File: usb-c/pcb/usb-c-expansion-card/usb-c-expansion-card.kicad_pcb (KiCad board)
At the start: 4 copper layers, 26 x 30 mm, 15 parts, among them J1 USB_C_Receptacle, P1 USB_C_Plug, U1 USBLC6-2SC6, U2 USBLC6-2SC6, U3 USBLC6-2SC6

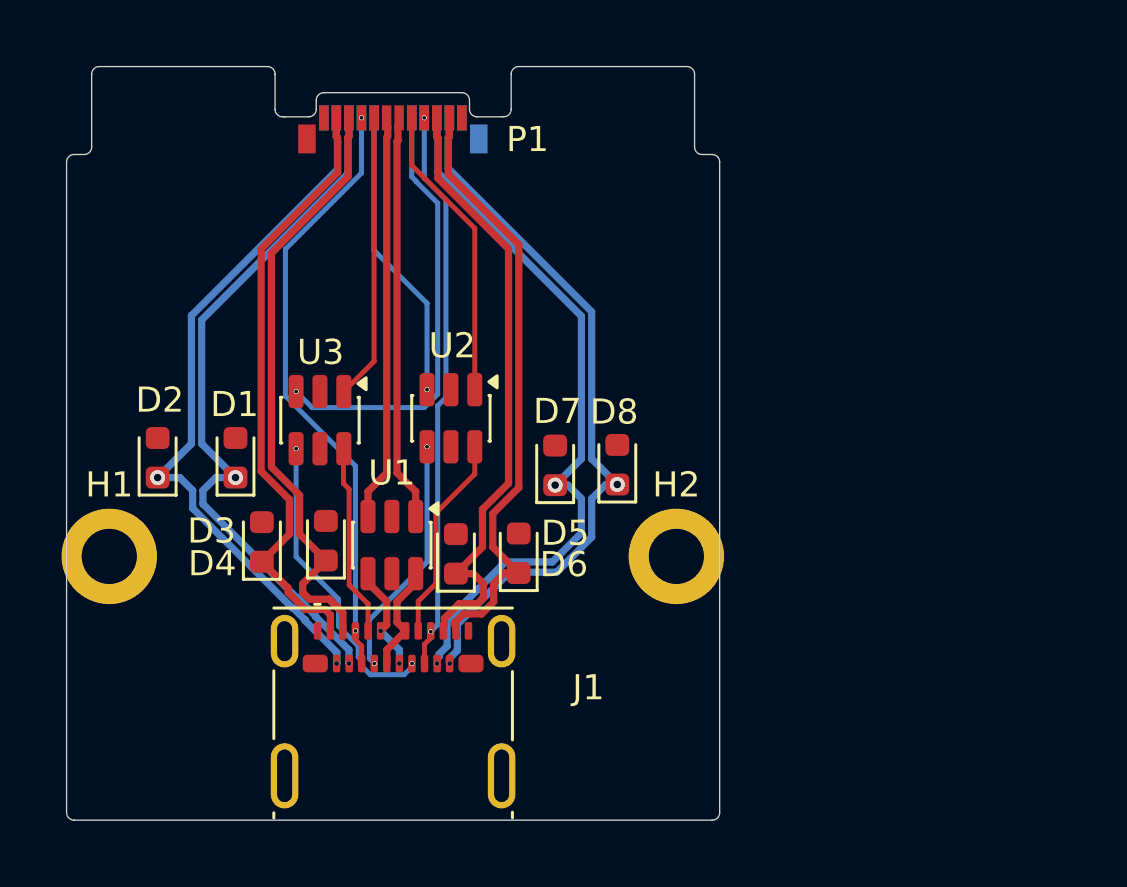
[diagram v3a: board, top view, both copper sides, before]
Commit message: routing corrected after moving footprints
Board outline was malformed, which meant moving some
stuff around and changing some traces

Signed-off-by: Lucy <user@domain.tld>
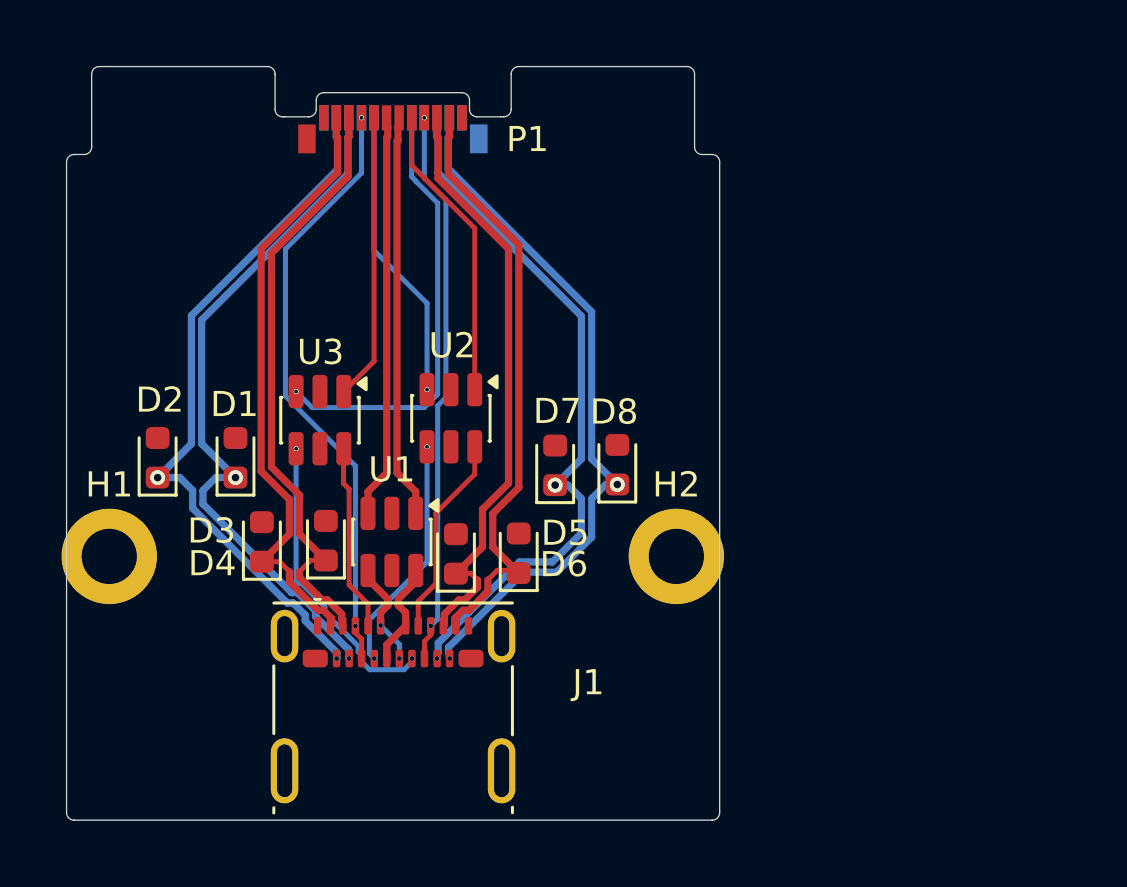
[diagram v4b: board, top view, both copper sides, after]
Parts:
- moved J1 0.20 mm to (140.0, 152.5)
- moved U1 0.12 mm to (139.9, 145.9)
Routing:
- net /ESD_RX2_N: track 24.4 -> 23.7 mm
- net /ESD_TX1_N: track 24.6 -> 24.0 mm
- net /ESD_TX2_N: track 28.8 -> 28.2 mm

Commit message: Only silkscreen graphics/text and vias missing
Signed-off-by: Lucy <user@domain.tld>
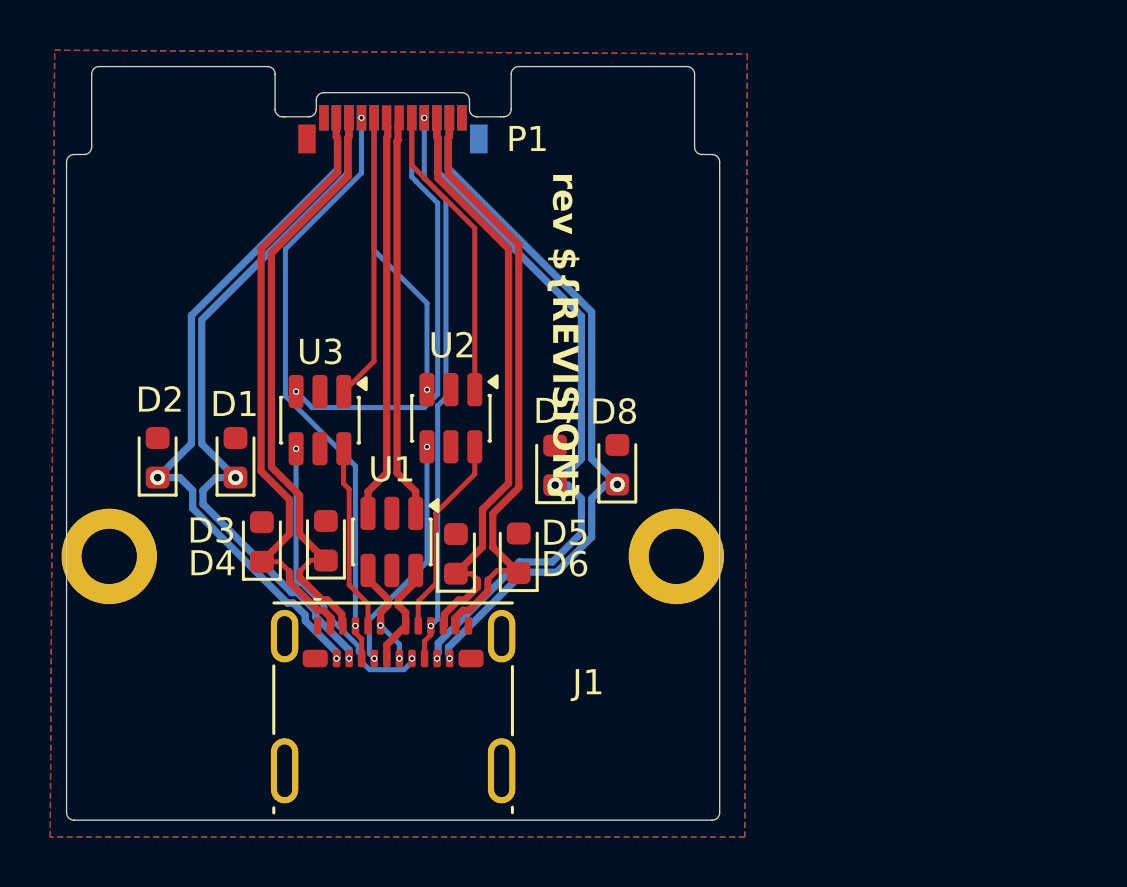
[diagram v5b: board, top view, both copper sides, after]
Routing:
- added copper zone on B.Cu, net GND
- added copper zone on F.Cu, net GND
- added copper zone on In1.Cu, net GND
- added copper zone on In2.Cu, net GND
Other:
- board text added: "rev ${REVISION}"

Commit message: Add text and graphics to silkscreen
Signed-off-by: Lucy <user@domain.tld>
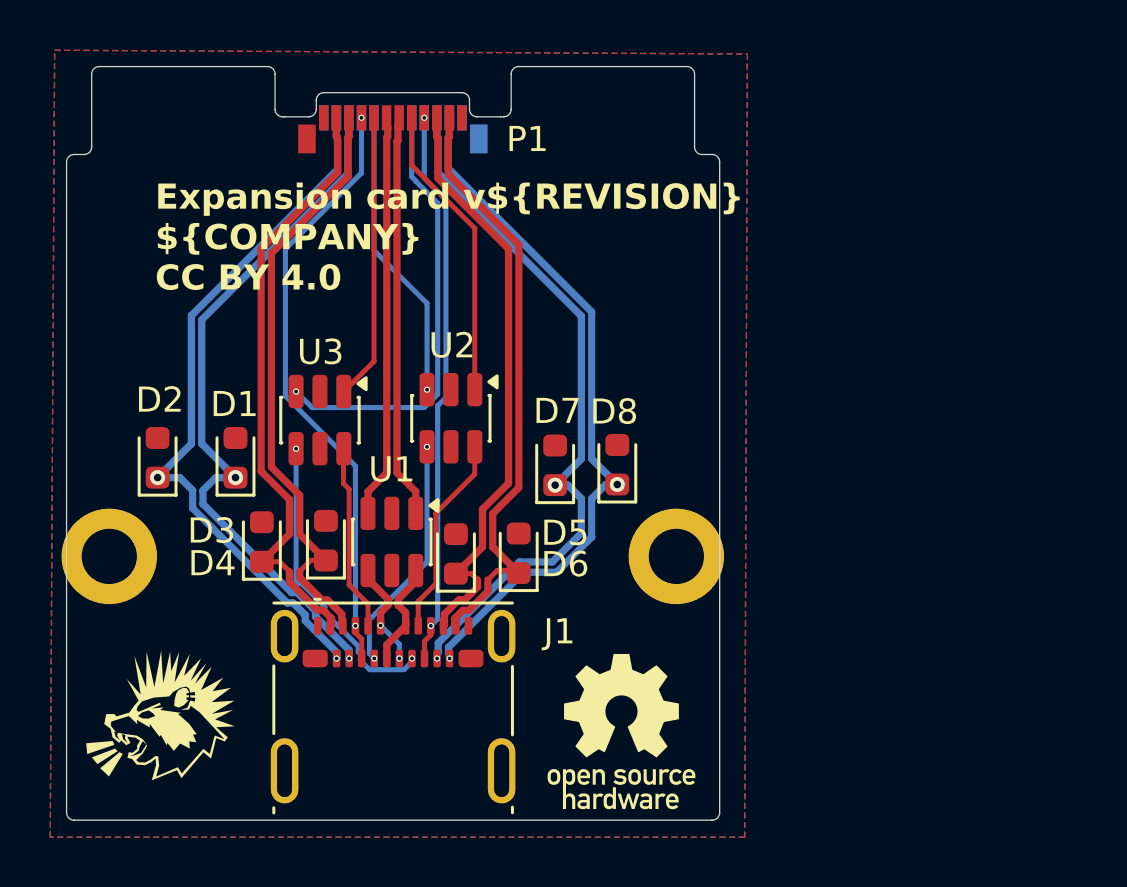
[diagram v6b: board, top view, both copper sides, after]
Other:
- board text added: "Expansion card v${REVISION} ${COMPANY} CC BY 4.0"
- board text removed: "rev ${REVISION}"

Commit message: minor text adjustments (silkscreen)
Signed-off-by: Lucy <user@domain.tld>
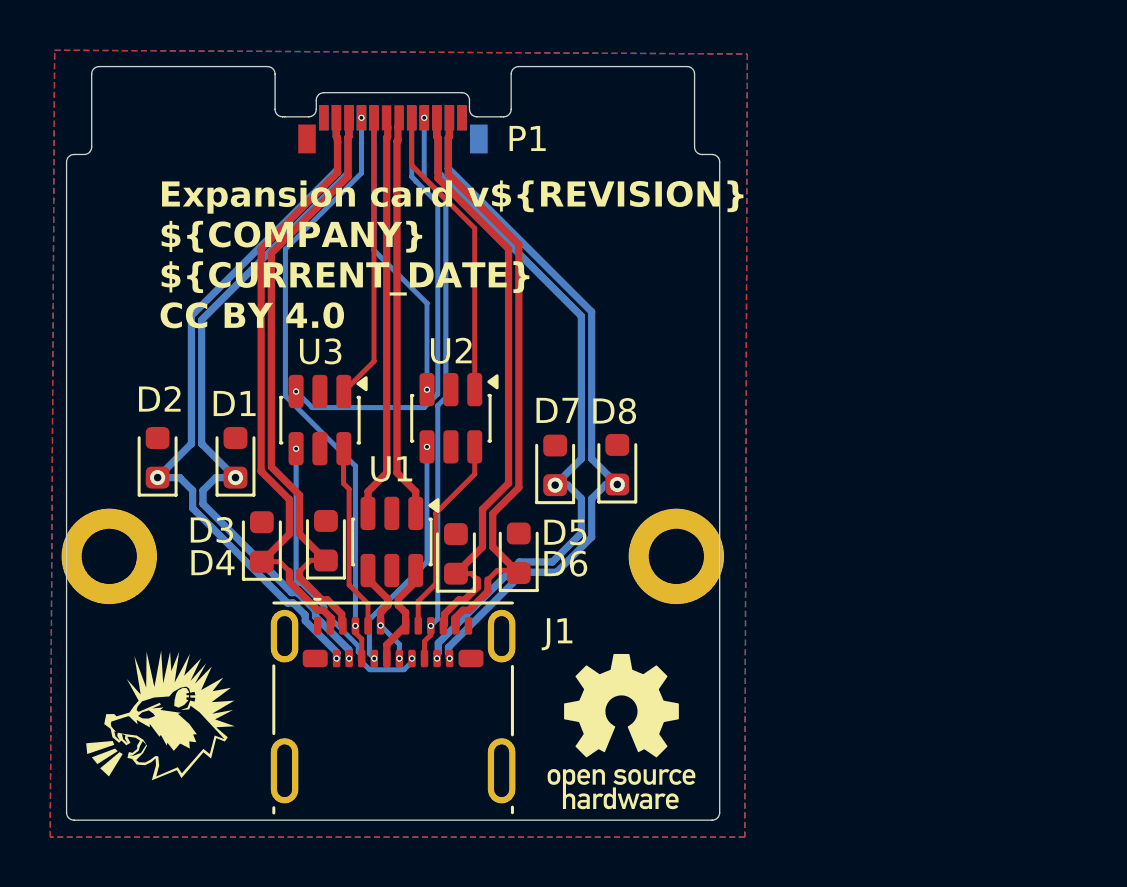
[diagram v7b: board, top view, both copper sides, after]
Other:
- board text added: "Expansion card v${REVISION} ${COMPANY} ${CURRENT_DATE} CC BY 4.0"
- board text removed: "Expansion card v${REVISION} ${COMPANY} CC BY 4.0"
